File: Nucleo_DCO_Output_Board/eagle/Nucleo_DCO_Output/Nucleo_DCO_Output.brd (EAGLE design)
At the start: 94 x 71.1 mm, 38 parts, among them CN1 9VPWR, IC1 TLE2426LP, IC2 NJM4580, IC3 NJM4580

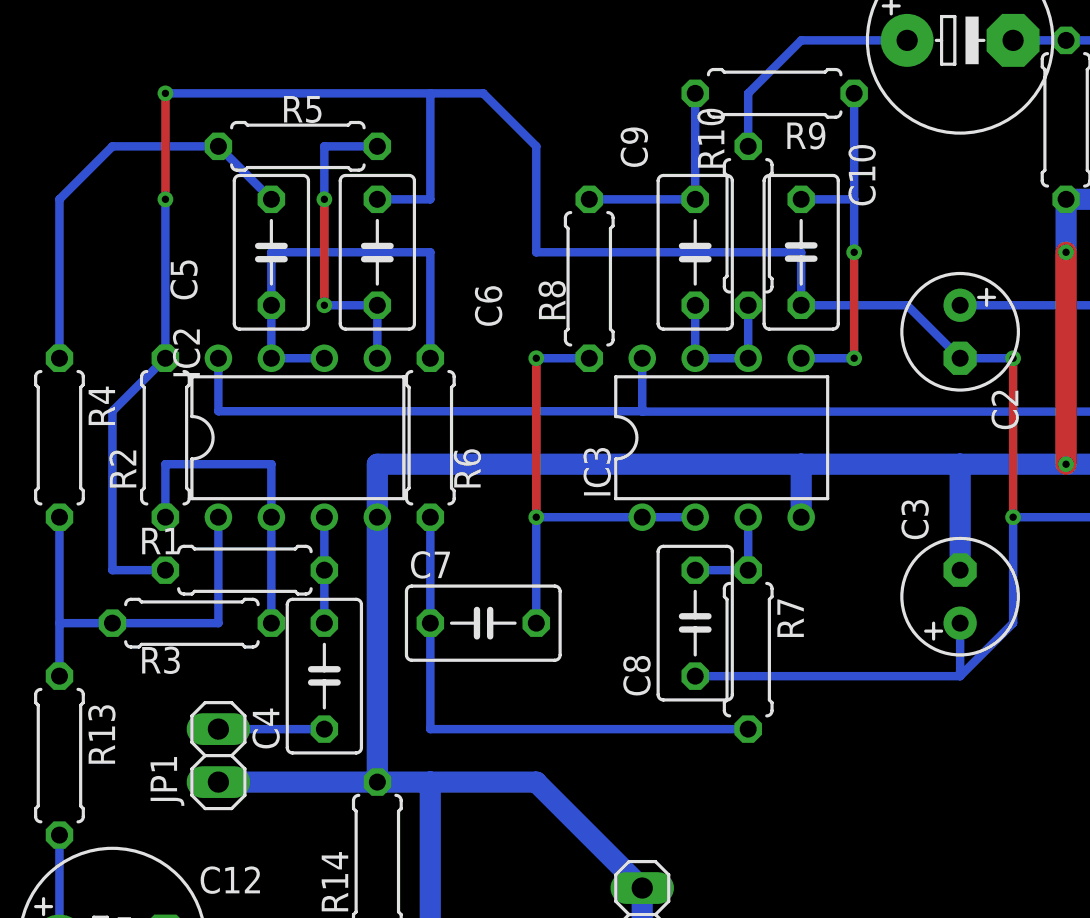
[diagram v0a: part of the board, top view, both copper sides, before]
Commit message: Update: Nucleo_DCO_Output (add de-coupling cap)
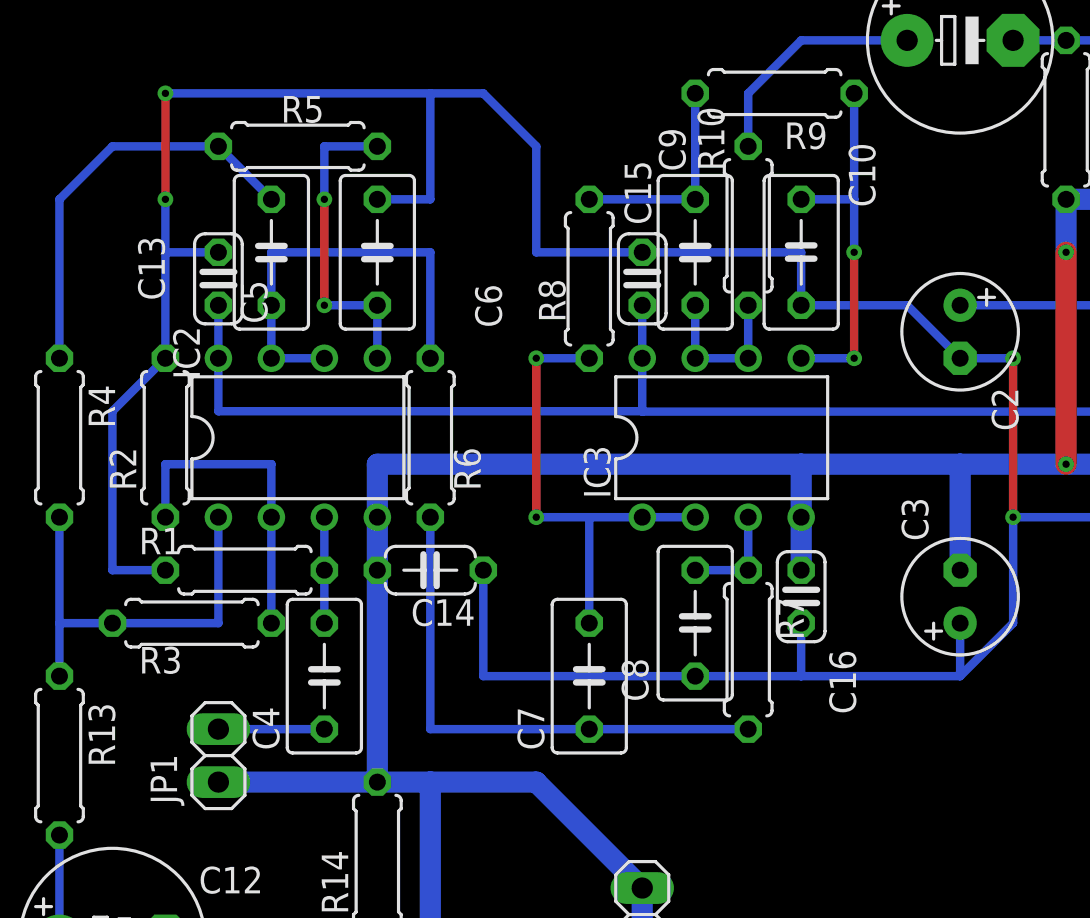
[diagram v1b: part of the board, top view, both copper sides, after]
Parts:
- added C13, C15, C16: 0.1uF, rcl:C025-024X044
- added C14: 0.1uF, rcl:C050-024X044
- moved C7 5.68 mm to (40.6, 27.9), turned to 90 degrees
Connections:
- net GND: now also C14.2, C16.2
- net VCC: now also C13.1, C15.1
- net VCC/2: now also C13.2, C14.1, C15.2, C16.1
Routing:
- net VCC/2: track 123.6 -> 143.9 mm
- net VCC: track 98.8 -> 103.8 mm
- net GND: track 161.8 -> 164.3 mm
